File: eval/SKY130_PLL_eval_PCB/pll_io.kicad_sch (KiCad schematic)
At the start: 15 parts, among them J14 142-0701-851_TO_SENSO1, U3 AD8000YCPZ-REEL7

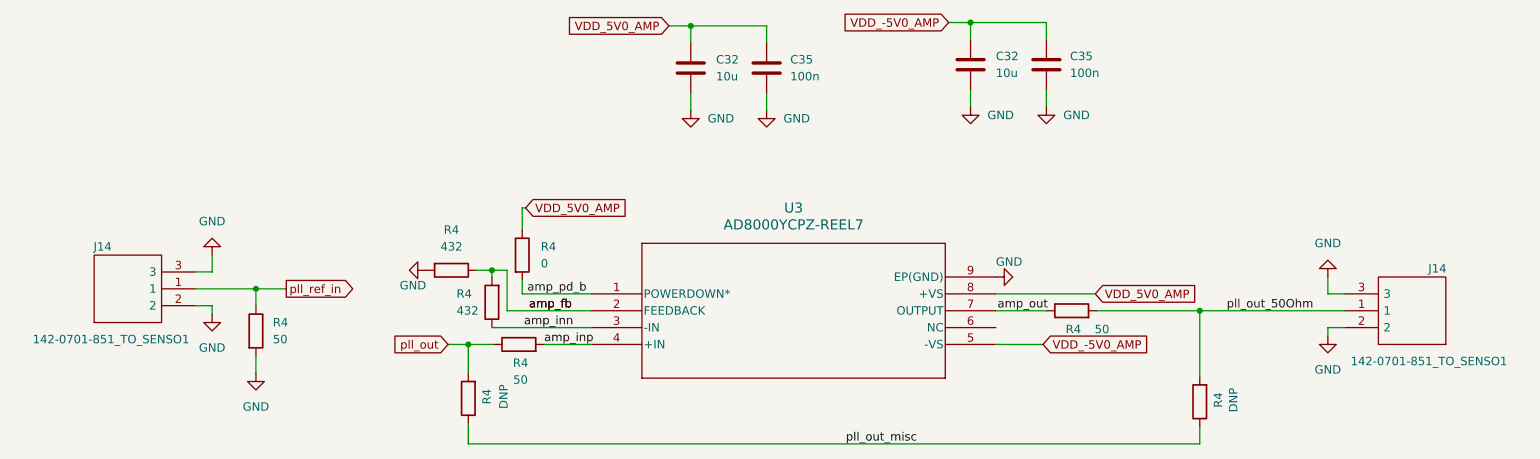
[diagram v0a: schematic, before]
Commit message: eval pcb added
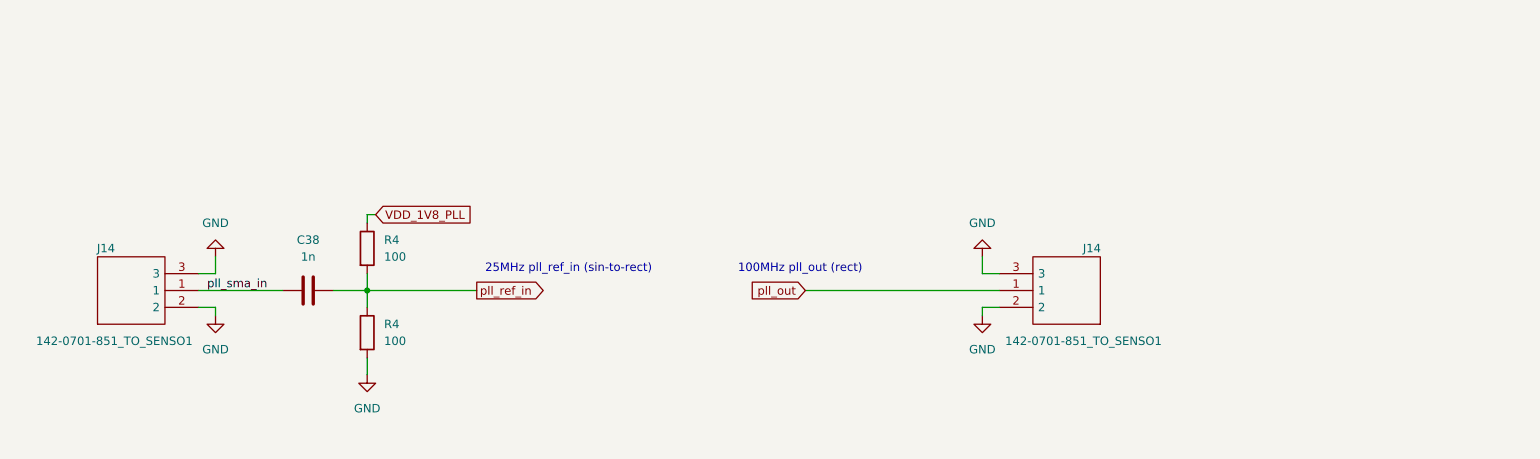
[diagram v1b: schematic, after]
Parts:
- removed C32 (x2): 10u, Capacitor_SMD:C_0603_1608Metric, symbol Device:C
- removed C35 (x2): 100n, Capacitor_SMD:C_0603_1608Metric, symbol Device:C
- removed R4 (x2): 432, Capacitor_SMD:C_0603_1608Metric, symbol Device:R
- removed R4 (x2): DNP, Capacitor_SMD:C_0603_1608Metric, symbol Device:R
- removed R4 (x2): 50, Capacitor_SMD:C_0603_1608Metric, symbol Device:R
- removed R4: 0, Capacitor_SMD:C_0603_1608Metric, symbol Device:R
- removed U3: AD8000YCPZ-REEL7, ad8000ycpz:CP_8_13_ADI, symbol ad8000ycpz:AD8000YCPZ-REEL7
- added C38: 1n, Capacitor_SMD:C_0603_1608Metric, symbol Device:C
- added R4: 100, Capacitor_SMD:C_0603_1608Metric, symbol Device:R
- R4: value 50 -> 100
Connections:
- net pll_out_50Ohm is gone; now on net pll_out: J14.1
- net pll_ref_in: now also C38.2, R4.2; no longer J14.1
- new net VDD_1V8_PLL: R4.1
- new net pll_sma_in: C38.1, J14.1
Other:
- note added: "100MHz pll_out (rect)"
- note added: "25MHz pll_ref_in (sin-to-rect)"
- moved on the sheet: J14, R4

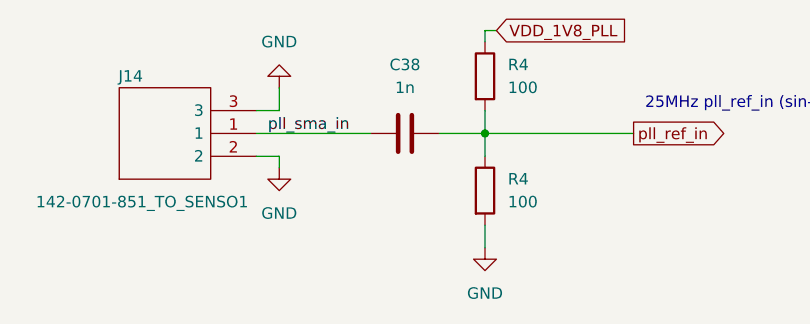
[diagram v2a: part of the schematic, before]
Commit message: digital design evaluation added
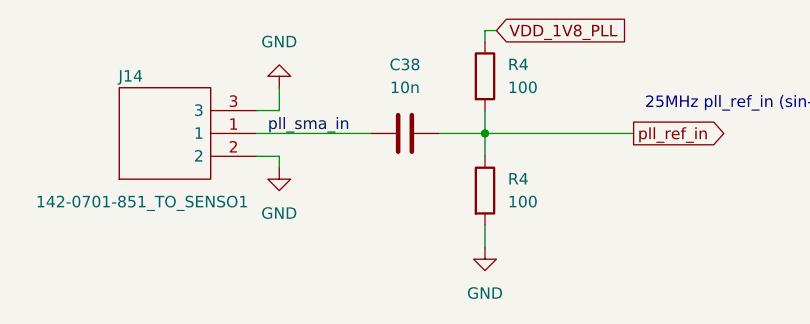
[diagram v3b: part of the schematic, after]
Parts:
- C38: value 1n -> 10n
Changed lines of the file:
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@@
 			)
 		)
-		(property "Value" "1n"
+		(property "Value" "10n"
 			(at 66.04 96.52 90)
 			(effects
